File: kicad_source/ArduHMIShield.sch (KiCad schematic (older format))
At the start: 49 parts, among them CN1 ARDUINO_ISP, Q1 2N7002, SW1 TAST_VER, SW2 TAST_VER, SW3 TAST_VER, SW4 TAST_VER, SW5 TAST_VER, SW6 TAST_VER, U1 LT1117, U2 74VHC245D

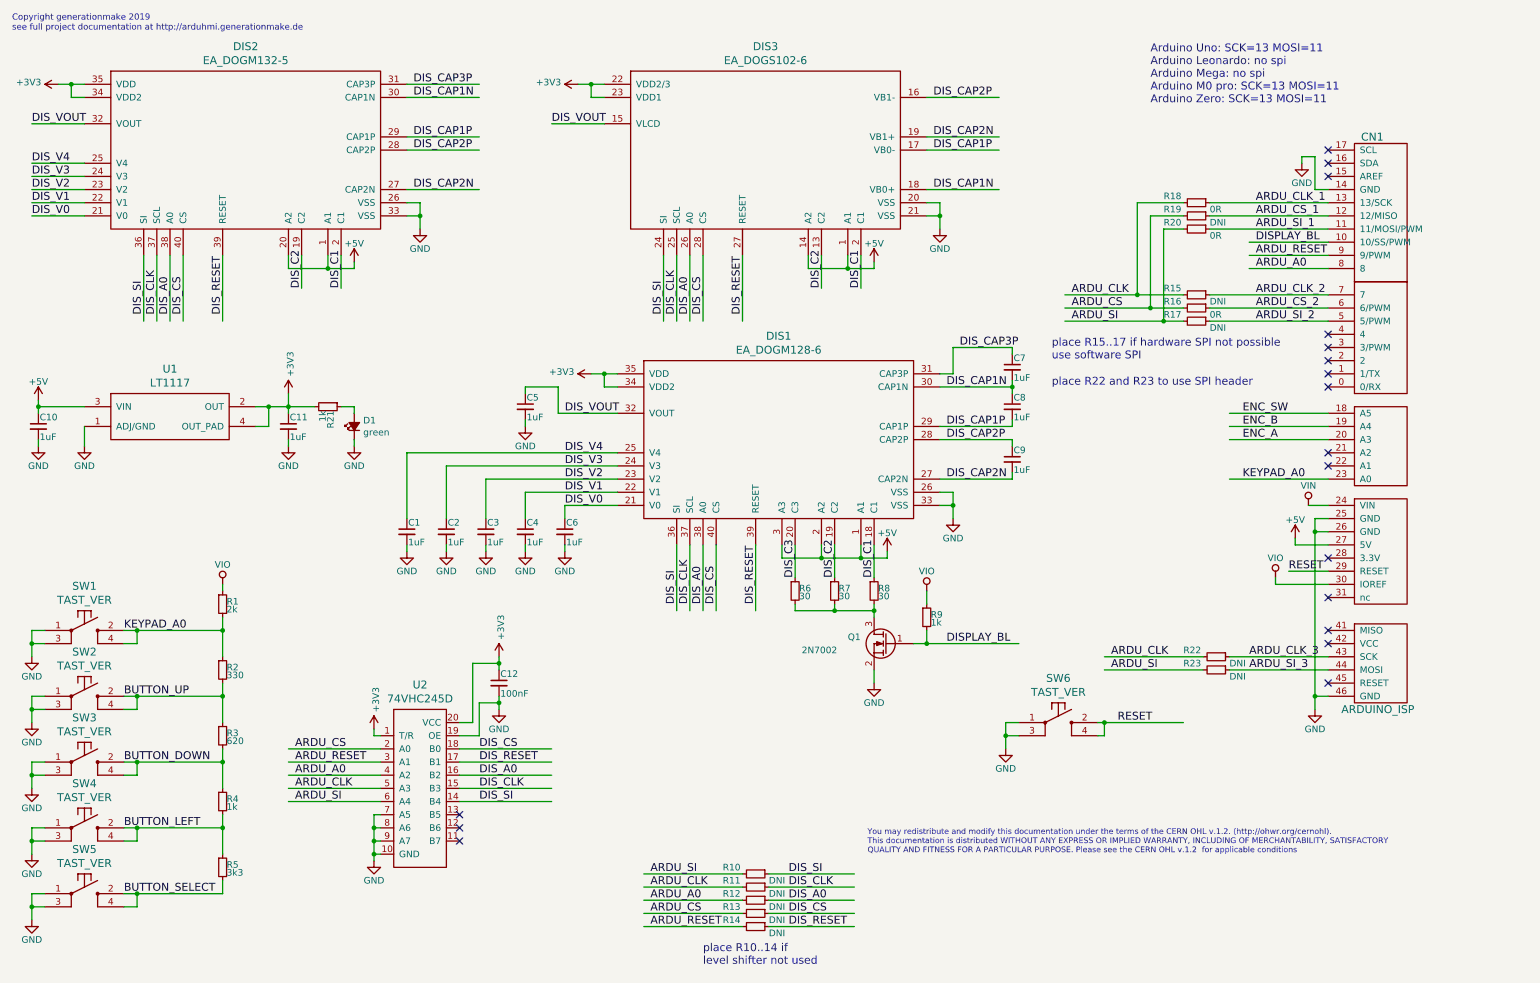
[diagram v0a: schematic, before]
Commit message: added Arduino MKR conector
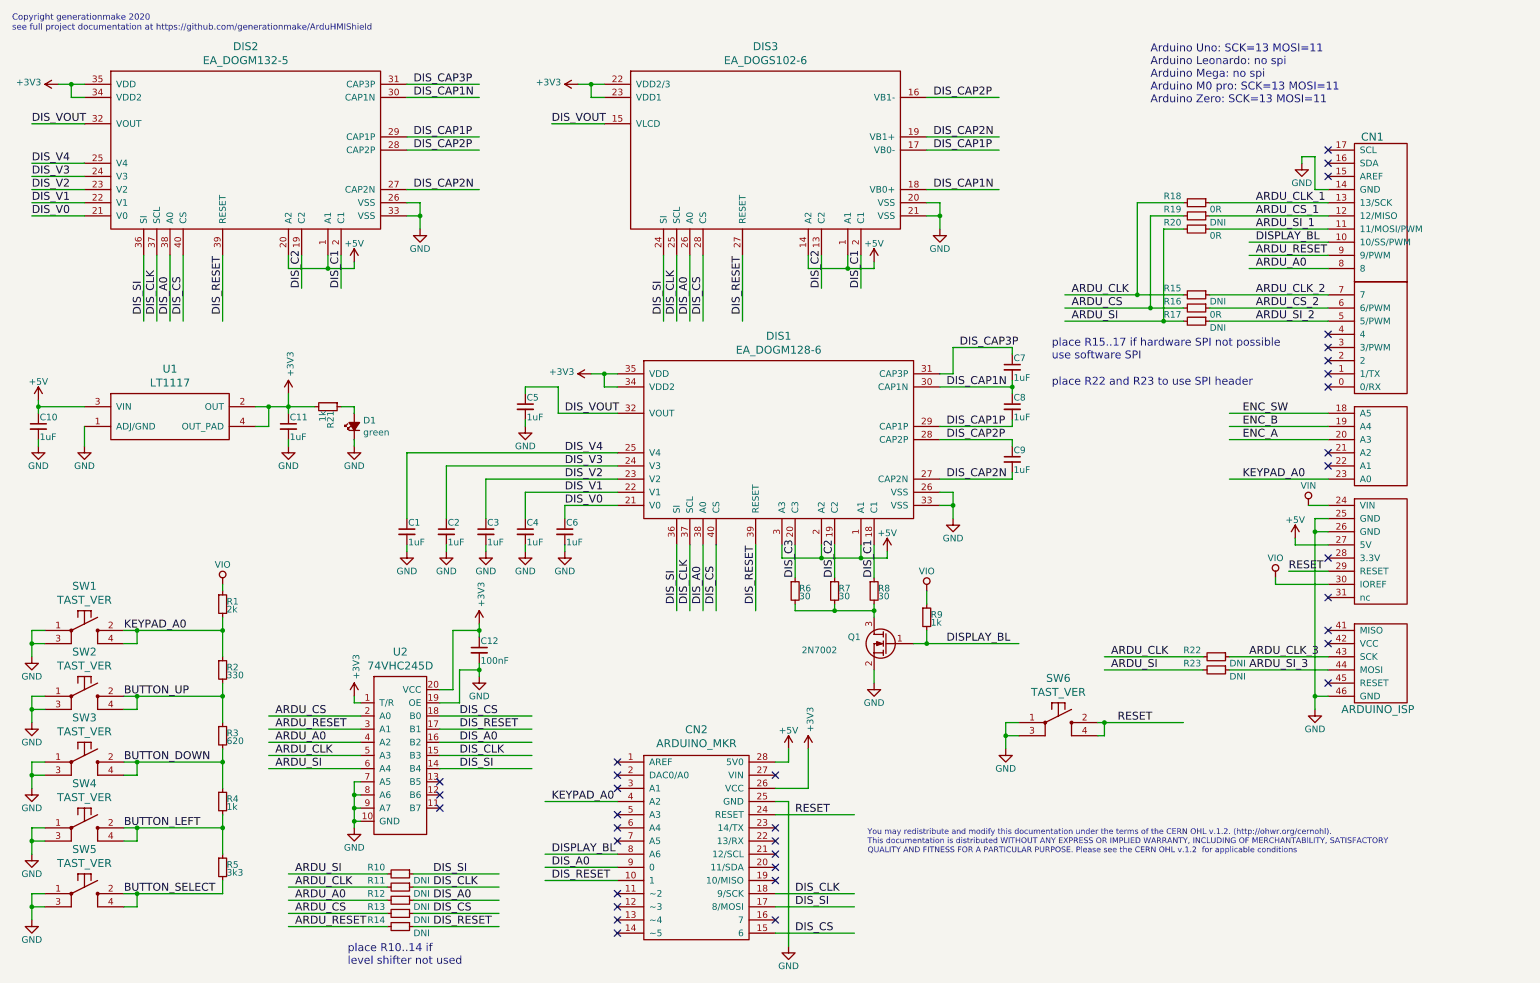
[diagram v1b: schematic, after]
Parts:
- added CN2: ARDUINO_MKR, MODULE_compute:ARDUINO_MKR, symbol MODULE_compute:ARDUINO_MKR
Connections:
- wire segments 282 -> 296
- no-connect marks 18 -> 35
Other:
- note added: "Copyright generationmake 2020\nsee full project documentation at https://github.com/generationmake/ArduHMIShield"
- note removed: "Copyright generationmake 2019\nsee full project documentation at http://arduhmi.generationmake.de"
- moved on the sheet: C12, R10, R11, R12, R13, R14, U2

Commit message: added holes for MKR connector
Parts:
- added L1, L2: Label, labels:generationmake_logo, symbol devices:Label
- CN2: footprint MODULE_compute:ARDUINO_MKR -> MODULE_compute:ARDUINO_MKR_HOLES
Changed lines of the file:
@@
 	1    0    0    -1
 $EndComp
-Text Notes 9150 1300 0    60   ~ 0
+Text Notes 8800 1300 0    60   ~ 0
 Arduino Uno: SCK=13 MOSI=11\nArduino Leonardo: no spi\nArduino Mega: no spi\nArduino M0 pro: SCK=13 MOSI=11\nArduino Zero: SCK=13 MOSI=11\n\n
 $Comp
@@
 F 0 "CN2" H 5700 7747 60  0000 C CNN
 F 1 "ARDUINO_MKR" H 5700 7641 60  0000 C CNN
-F 2 "MODULE_compute:ARDUINO_MKR" H 5600 7500 60  0001 C CNN
+F 2 "MODULE_compute:ARDUINO_MKR_HOLES" H 5600 7500 60  0001 C CNN
 F 3 "" H 5700 6550 60  0000 C CNN
 	1    5700 6850
@@
 NoConn ~ 5100 6300
 NoConn ~ 5100 6400
+$Comp
+L devices:Label L1
+U 1 1 5F4DC93F
+P 10700 650
+F 0 "L1" H 10928 703 60  0000 L CNN
+F 1 "Label" H 10928 597 60  0000 L CNN
+F 2 "labels:generationmake_logo" H 10928 544 60  0001 L CNN
+F 3 "" H 10700 650 60  0000 C CNN
+	1    10700 650
+	1    0    0    -1
+$EndComp
+$Comp
+L devices:Label L2
+U 1 1 5F4DD031
+P 10700 1000
+F 0 "L2" H 10928 1053 60  0000 L CNN
+F 1 "Label" H 10928 947 60  0000 L CNN
+F 2 "labels:generationmake_logo" H 10928 894 60  0001 L CNN
+F 3 "" H 10700 1000 60  0000 C CNN
+	1    10700 1000
+	1    0    0    -1
+$EndComp
 $EndSCHEMATC

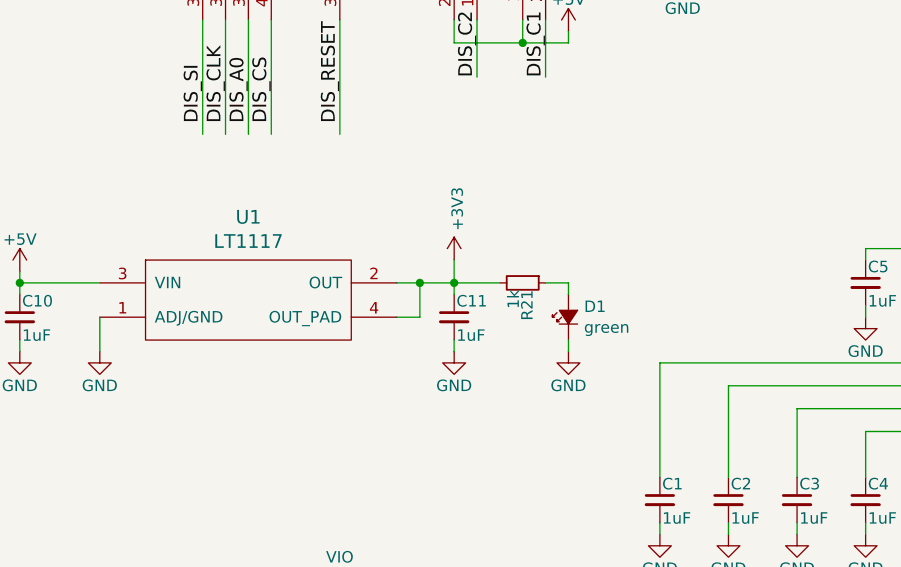
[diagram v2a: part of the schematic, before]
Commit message: updated order numbers
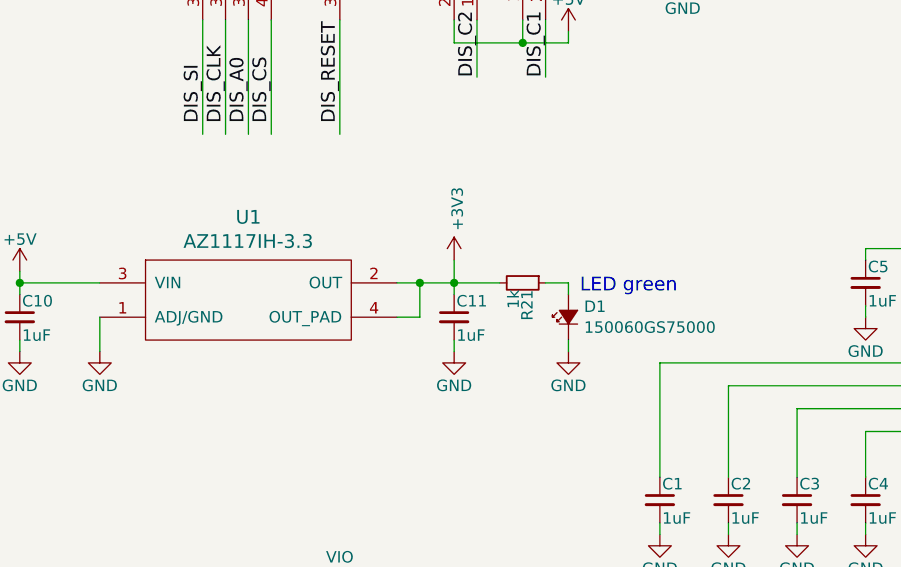
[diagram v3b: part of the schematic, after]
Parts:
- D1: value green -> 150060GS75000
- U1: value LT1117 -> AZ1117IH-3.3
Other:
- note added: "LED green"
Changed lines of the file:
@@
 P 1700 3600
 F 0 "U1" H 1700 3987 60  0000 C CNN
-F 1 "LT1117" H 1700 3881 60  0000 C CNN
+F 1 "AZ1117IH-3.3" H 1700 3881 60  0000 C CNN
 F 2 "SOT_TO:SOT-223" H 1650 3300 60  0001 C CNN
 F 3 "" H 1700 3600 60  0000 C CNN
@@
 P 3100 3650
 F 0 "D1" V 3146 3582 50  0000 R CNN
-F 1 "green" V 3055 3582 50  0000 R CNN
+F 1 "150060GS75000" V 3055 3582 50  0000 R CNN
 F 2 "LEDs:LED_0603" V 3100 3650 50  0001 C CNN
 F 3 "" V 3100 3650 50  0000 C CNN
@@
 	1    0    0    -1
 $EndComp
+Text Notes 3150 3550 0    60   ~ 0
+LED green
 $EndSCHEMATC
